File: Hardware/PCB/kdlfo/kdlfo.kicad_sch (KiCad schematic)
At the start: 31 parts, among them J1 3_pin_Molex_header, J10 AudioJack2, J11 3_pin_Molex_connector, J12 3_pin_Molex_connector, J13 3_pin_Molex_connector, J14 3_pin_Molex_connector, J15 Synth_power_2x5, J2 3_pin_Molex_header, J3 3_pin_Molex_header, J4 3_pin_Molex_header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

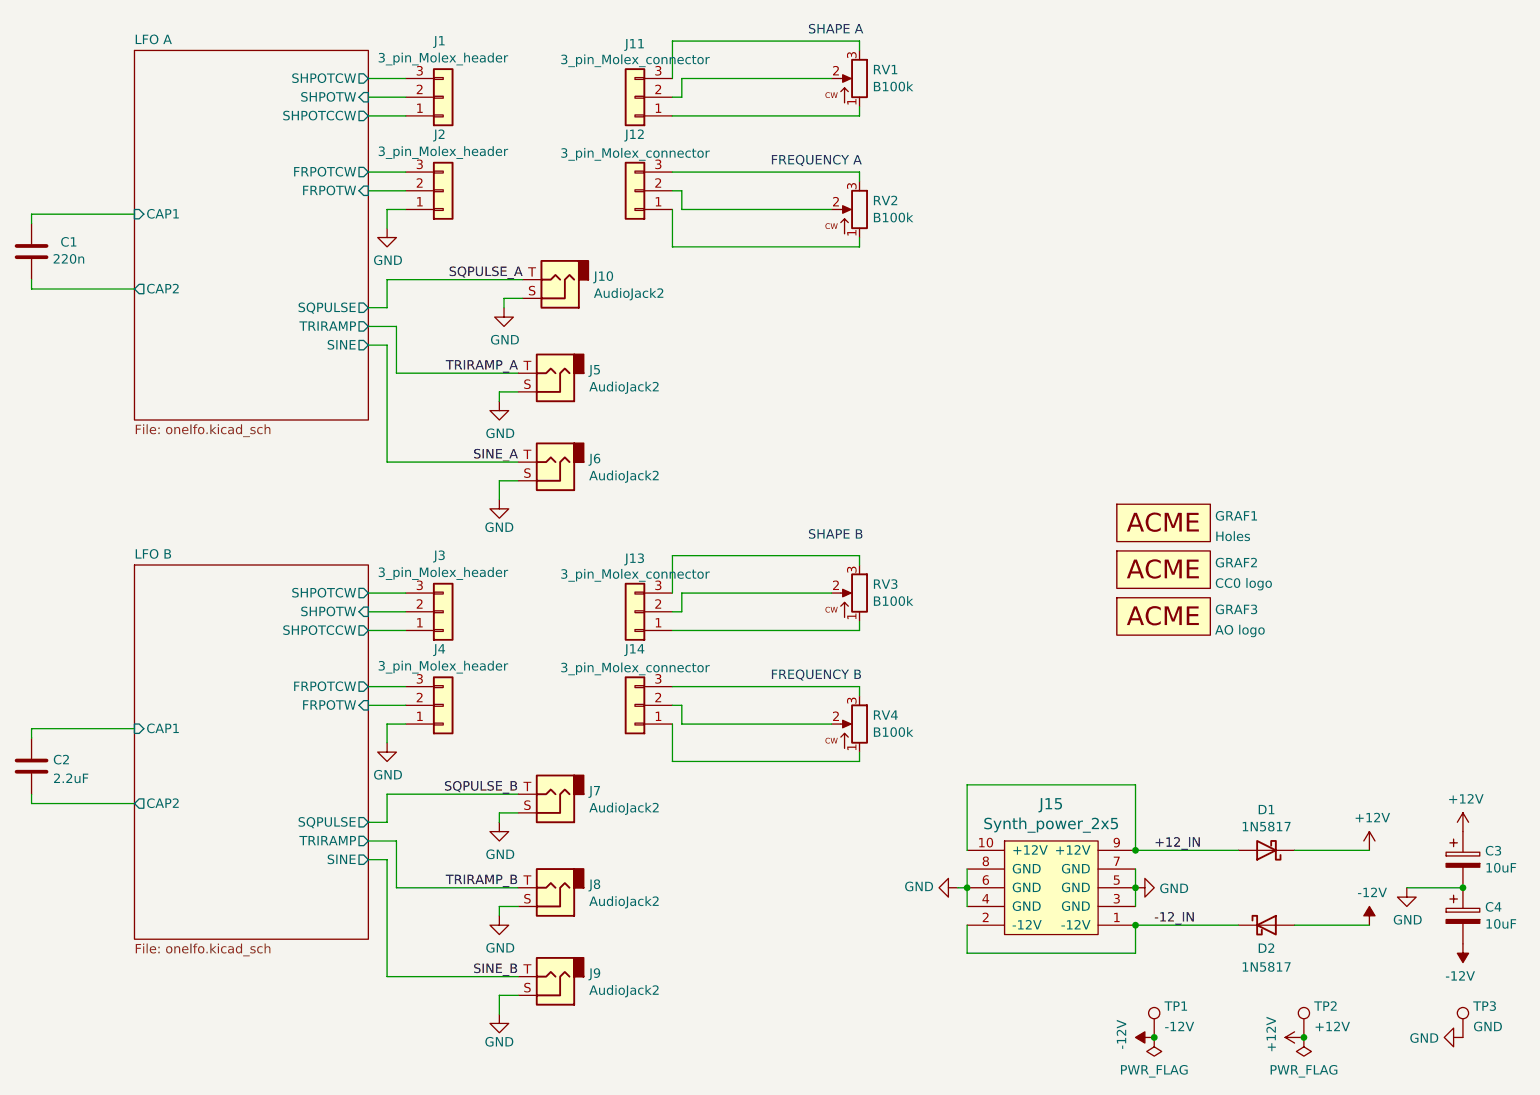
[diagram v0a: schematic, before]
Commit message: Fix silkscreen errors and omissions, change integ resistor, add shape resistor
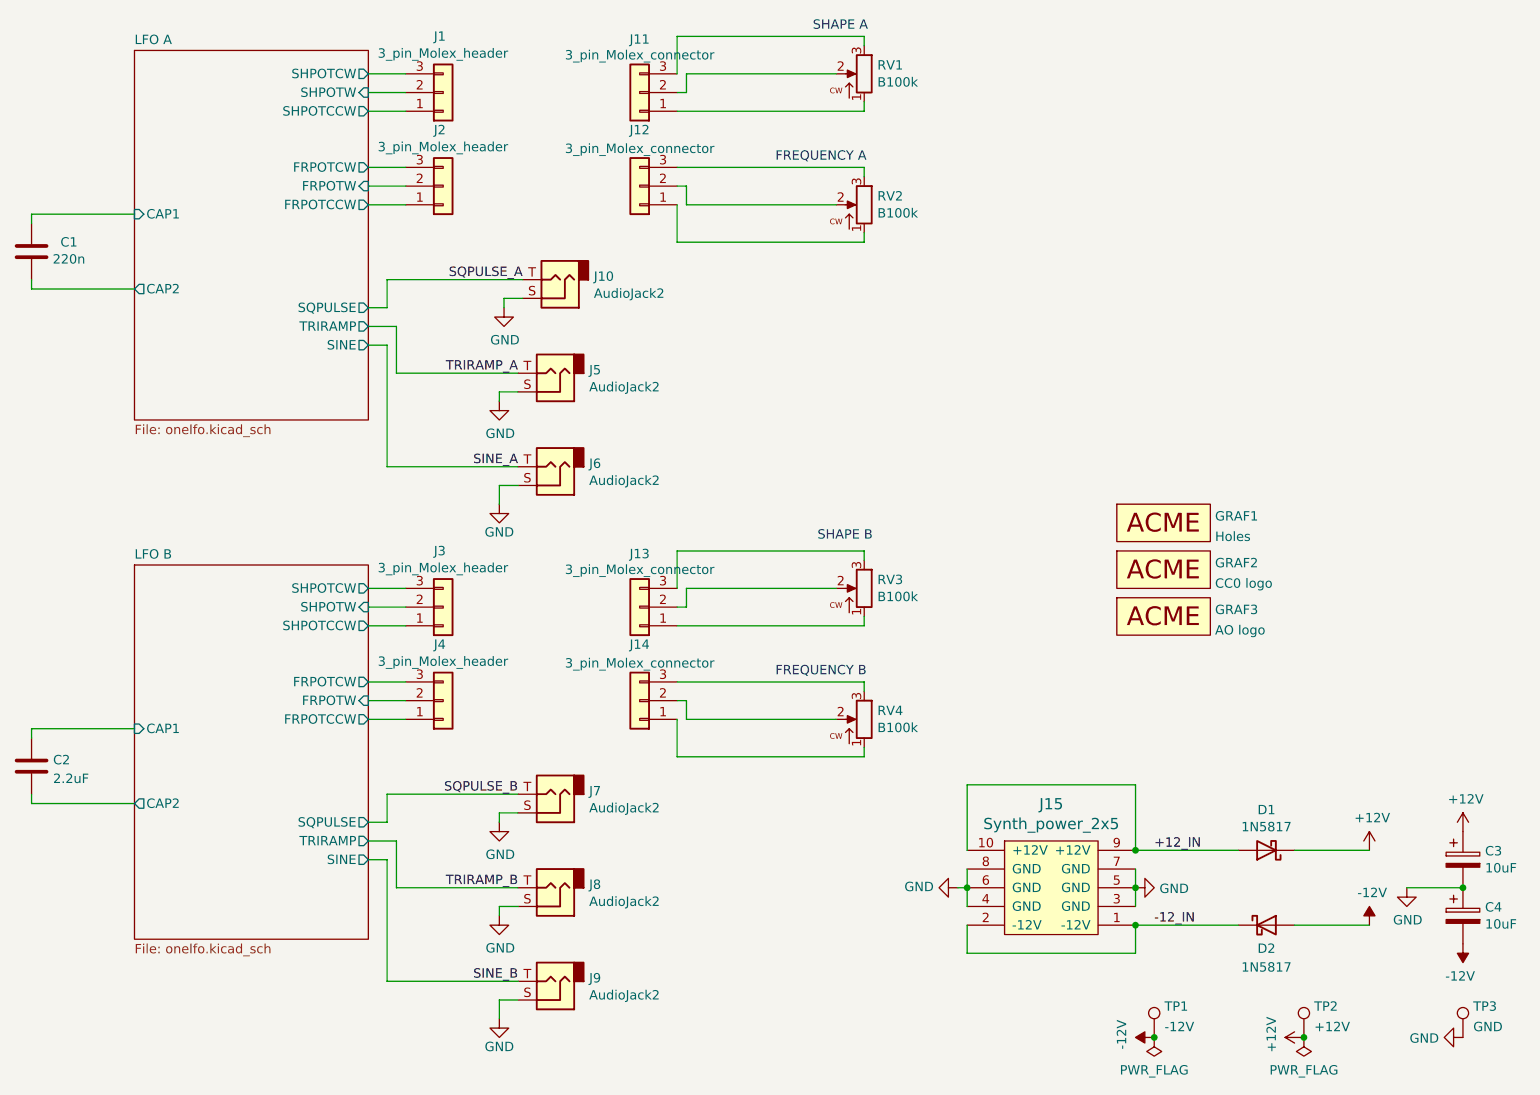
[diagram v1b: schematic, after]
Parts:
- C1: SKU A-984 -> (none); Vendor Tayda -> (none)
- C2: SKU A-4532 -> A-4223
- C3, C4: SKU A-4349 -> (none)
- D1, D2: SKU A-159 -> (none); Vendor Tayda -> (none)
- J10, J5, J6, J7, J8, J9: SKU A-1121 -> (none); Vendor Tayda -> (none)
- RV1, RV2, RV3, RV4: SKU A-1984 -> (none)
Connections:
- net GND: no longer J2.1 (Pin_1), J4.1 (Pin_1)
- new net LFO A/FRPOTCCW: J2.1 (Pin_1)
- new net LFO B/FRPOTCCW: J4.1 (Pin_1)
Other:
- sheet LFO A ports: added FRPOTCCW; removed none
- sheet LFO B ports: added FRPOTCCW; removed none
- moved on the sheet: J1, J11, J12, J13, J14, J2, J3, J4, J6, J9, RV1, RV2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
